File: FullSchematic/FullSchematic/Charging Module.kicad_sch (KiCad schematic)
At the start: 13 parts, among them J1 TP4056

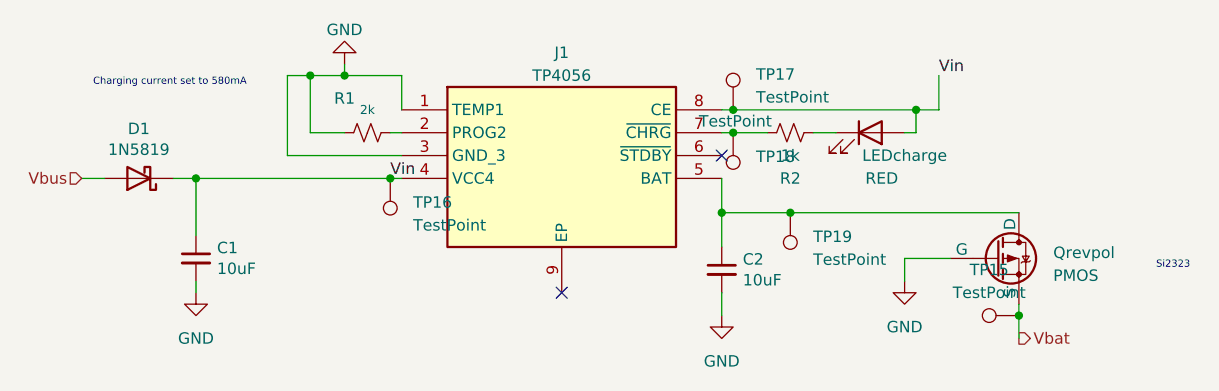
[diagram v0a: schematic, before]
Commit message: completed and generated BOM
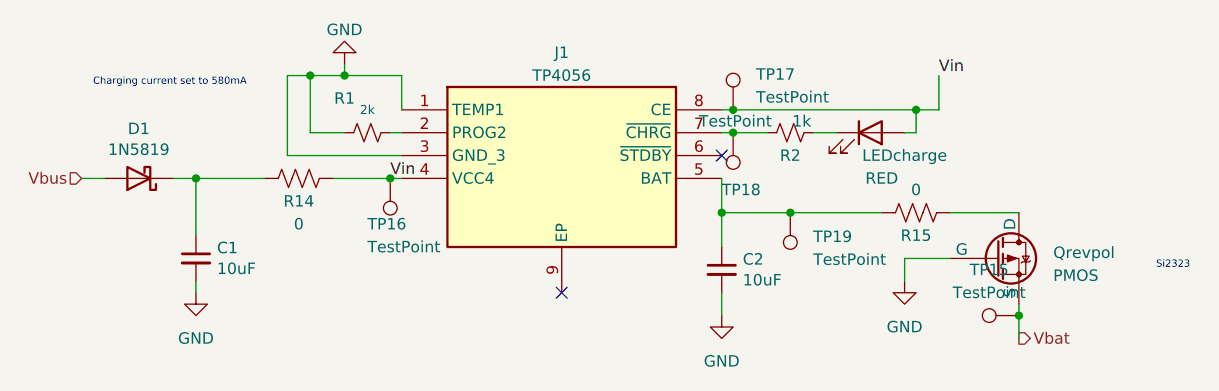
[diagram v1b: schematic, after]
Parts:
- added R14, R15: 0, symbol Device:R_US
- LEDcharge: Price 0.005 -> 0.01; Price ( 1 board) 0.005 -> 0.01; Price (5 boards) 0.025 -> 0.05
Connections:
- net Vin: now also R14.1; no longer C1.1, D1.1 (K)
- net at C2.1, J1.5 (BAT), TP19.1: now also R15.1; no longer Qrevpol.1 (D)
- new net: C1.1, D1.1 (K), R14.2
- new net: Qrevpol.1 (D), R15.2
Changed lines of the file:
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@@
   (junction (at 132.08 67.31) (diameter 0) (color 0 0 0 0)
   )
+  (junction (at 137.16 78.74) (diameter 0) (color 0 0 0 0)
+  )
+  (junction (at 207.01 93.98) (diameter 0) (color 0 0 0 0)
+  )
   (junction (at 181.61 82.55) (diameter 0) (color 0 0 0 0)
   )
-  (junction (at 207.01 93.98) (diameter 0) (color 0 0 0 0)
-  )
-  (junction (at 137.16 78.74) (diameter 0) (color 0 0 0 0)
-  )
   (junction (at 128.27 67.31) (diameter 0) (color 0 0 0 0)
   )
@@
   (junction (at 195.58 71.12) (diameter 0) (color 0 0 0 0)
   )
+  (junction (at 175.26 71.12) (diameter 0) (color 0 0 0 0)
+  )
   (junction (at 115.57 78.74) (diameter 0) (color 0 0 0 0)
-  )
-  (junction (at 175.26 71.12) (diameter 0) (color 0 0 0 0)
   )
   (no_connect (at 173.99 76.2))
@@
     (stroke (width 0) (type default))
   )
+  (wire (pts (xy 137.16 78.74) (xy 138.43 78.74))
+    (stroke (width 0) (type default))
+  )
   (wire (pts (xy 175.26 71.12) (xy 195.58 71.12))
     (stroke (width 0) (type default))
@@
     (stroke (width 0) (type default))
   )
+  (wire (pts (xy 115.57 78.74) (xy 123.19 78.74))
+    (stroke (width 0) (type default))
+  )
   (wire (pts (xy 195.58 73.66) (xy 195.58 71.12))
     (stroke (width 0) (type default))
   )
-  (wire (pts (xy 115.57 78.74) (xy 137.16 78.74))
-    (stroke (width 0) (type default))
-  )
   (wire (pts (xy 138.43 76.2) (xy 125.73 76.2))
     (stroke (width 0) (type default))
@@
     (stroke (width 0) (type default))
   )
+  (wire (pts (xy 199.39 82.55) (xy 207.01 82.55))
+    (stroke (width 0) (type default))
+  )
   (wire (pts (xy 113.03 78.74) (xy 115.57 78.74))
     (stroke (width 0) (type default))
@@
     (stroke (width 0) (type default))
   )
+  (wire (pts (xy 181.61 82.55) (xy 191.77 82.55))
+    (stroke (width 0) (type default))
+  )
   (wire (pts (xy 128.27 73.66) (xy 128.27 67.31))
     (stroke (width 0) (type default))
@@
     (stroke (width 0) (type default))
   )
-  (wire (pts (xy 181.61 82.55) (xy 207.01 82.55))
-    (stroke (width 0) (type default))
-  )
   (wire (pts (xy 194.31 90.17) (xy 194.31 87.63))
     (stroke (width 0) (type default))
@@
     (stroke (width 0) (type default))
   )
-  (wire (pts (xy 137.16 78.74) (xy 138.43 78.74))
+  (wire (pts (xy 130.81 78.74) (xy 137.16 78.74))
     (stroke (width 0) (type default))
   )
@@
     )
   )
+  (symbol (lib_id "Device:R_US") (at 127 78.74 270) (unit 1)
+    (in_bom yes) (on_board yes) (dnp no)
+    (property "Reference" "R14" (at 127 81.28 90)
+      (effects (font (size 1.27 1.27)))
+    )
+    (property "Value" "0" (at 127 83.82 90)
+      (effects (font (size 1.27 1.27)))
+    )
+    (property "Footprint" "" (at 126.746 79.756 90)
+      (effects (font (size 1.27 1.27)) hide)
+    )
+    (property "Datasheet" "~" (at 127 78.74 0)
+      (effects (font (size 1.27 1.27)) hide)
+    )
+    (property "JLCPCB Part #" "C17888" (at 127 78.74 0)
+      (effects (font (size 1.27 1.27)) hide)
+    )
+    (property "Price" "0.003" (at 127 78.74 0)
+      (effects (font (size 1.27 1.27)) hide)
+    )
+    (property "Price ( 1 board)" "0.012" (at 127 78.74 0)
+      (effects (font (size 1.27 1.27)) hide)
+    )
+    (property "Price (5 boards)" "0.06" (at 127 78.74 0)
+      (effects (font (size 1.27 1.27)) hide)
+    )
+    (pin "1")
+    (pin "2")
+    (instances
+      (project "FullSchematic"
+        (path "/5dd86611-a33d-45ee-946c-01c599f30b12/58d1f368-4b84-4dfe-a353-084728cf6b07/00000000-0000-0000-0000-0000640501de"
+          (reference "R14") (unit 1)
+        )
+      )
+    )
+  )
   (symbol (lib_id "Device:LED") (at 190.5 73.66 0) (unit 1)
     (in_bom yes) (on_board yes) (dnp no)
@@
       (effects (font (size 1.27 1.27)) hide)
     )
-    (property "Price ( 1 board)" "0.005" (at 190.5 73.66 0)
-      (effects (font (size 1.27 1.27)) hide)
-    )
-    (property "Price (5 boards)" "0.025" (at 190.5 73.66 0)
+    (property "Price ( 1 board)" "0.01" (at 190.5 73.66 0)
+      (effects (font (size 1.27 1.27)) hide)
+    )
+    (property "Price (5 boards)" "0.05" (at 190.5 73.66 0)
       (effects (font (size 1.27 1.27)) hide)
     )
@@
       (effects (font (size 1.27 1.27)) hide)
     )
-    (property "Price" "0.005" (at 190.5 73.66 0)
+    (property "Price" "0.01" (at 190.5 73.66 0)
       (effects (font (size 1.27 1.27)) hide)
     )
@@
   )
   (symbol (lib_id "Connector:TestPoint") (at 137.16 78.74 180) (unit 1)
-    (in_bom yes) (on_board yes) (dnp no) (fields_autoplaced)
-    (property "Reference" "TP16" (at 139.7 81.407 0)
+    (in_bom yes) (on_board yes) (dnp no)
+    (property "Reference" "TP16" (at 134.62 83.82 0)
       (effects (font (size 1.27 1.27)) (justify right))
     )
-    (property "Value" "TestPoint" (at 139.7 83.947 0)
+    (property "Value" "TestPoint" (at 134.62 86.36 0)
       (effects (font (size 1.27 1.27)) (justify right))
     )
@@
     )
   )
+  (symbol (lib_id "Device:R_US") (at 195.58 82.55 90) (unit 1)
+    (in_bom yes) (on_board yes) (dnp no)
+    (property "Reference" "R15" (at 195.58 85.09 90)
+      (effects (font (size 1.27 1.27)))
+    )
+    (property "Value" "0" (at 195.58 80.01 90)
+      (effects (font (size 1.27 1.27)))
+    )
+    (property "Footprint" "" (at 195.834 81.534 90)
+      (effects (font (size 1.27 1.27)) hide)
+    )
+    (property "Datasheet" "~" (at 195.58 82.55 0)
+      (effects (font (size 1.27 1.27)) hide)
+    )
+    (property "JLCPCB Part #" "C17888" (at 195.58 82.55 0)
+      (effects (font (size 1.27 1.27)) hide)
+    )
+    (property "Price" "0.003" (at 195.58 82.55 0)
+      (effects (font (size 1.27 1.27)) hide)
+    )
+    (property "Price ( 1 board)" "0.012" (at 195.58 82.55 0)
+      (effects (font (size 1.27 1.27)) hide)
+    )
+    (property "Price (5 boards)" "0.06" (at 195.58 82.55 0)
+      (effects (font (size 1.27 1.27)) hide)
+    )
+    (pin "1")
+    (pin "2")
+    (instances
+      (project "FullSchematic"
+        (path "/5dd86611-a33d-45ee-946c-01c599f30b12/58d1f368-4b84-4dfe-a353-084728cf6b07/00000000-0000-0000-0000-0000640501de"
+          (reference "R15") (unit 1)
+        )
+      )
+    )
+  )
   (symbol (lib_id "power:GND") (at 115.57 91.44 0) (unit 1)
     (in_bom yes) (on_board yes) (dnp no) (fields_autoplaced)
@@
   (symbol (lib_id "Device:R_Small_US") (at 181.61 73.66 90) (unit 1)
     (in_bom yes) (on_board yes) (dnp no)
-    (property "Reference" "R2" (at 181.61 78.74 90)
-      (effects (font (size 1.27 1.27)))
-    )
-    (property "Value" "1k" (at 181.61 76.2 90)
+    (property "Reference" "R2" (at 181.61 76.2 90)
+      (effects (font (size 1.27 1.27)))
+    )
+    (property "Value" "1k" (at 182.88 72.39 90)
       (effects (font (size 1.27 1.27)))
     )
@@
   (symbol (lib_id "Connector:TestPoint") (at 175.26 73.66 180) (unit 1)
     (in_bom yes) (on_board yes) (dnp no)
-    (property "Reference" "TP18" (at 177.8 76.327 0)
+    (property "Reference" "TP18" (at 173.99 80.01 0)
       (effects (font (size 1.27 1.27)) (justify right))
     )

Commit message: added more footprints
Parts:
- R14, R15: footprint (none) -> SpecificFootprints:RESC2013X65N
- TP15, TP16, TP17, TP18, TP19: footprint (none) -> TestPoint:TestPoint_Pad_D2.0mm
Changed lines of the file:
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@@
       (effects (font (size 1.27 1.27)))
     )
-    (property "Footprint" "" (at 126.746 79.756 90)
+    (property "Footprint" "SpecificFootprints:RESC2013X65N" (at 126.746 79.756 90)
       (effects (font (size 1.27 1.27)) hide)
     )
@@
       (effects (font (size 1.27 1.27)) (justify left))
     )
-    (property "Footprint" "" (at 180.34 71.12 0)
+    (property "Footprint" "TestPoint:TestPoint_Pad_D2.0mm" (at 180.34 71.12 0)
       (effects (font (size 1.27 1.27)) hide)
     )
@@
       (effects (font (size 1.27 1.27)) (justify right))
     )
-    (property "Footprint" "" (at 132.08 78.74 0)
+    (property "Footprint" "TestPoint:TestPoint_Pad_D2.0mm" (at 132.08 78.74 0)
       (effects (font (size 1.27 1.27)) hide)
     )
@@
       (effects (font (size 1.27 1.27)))
     )
-    (property "Footprint" "" (at 207.01 88.9 0)
+    (property "Footprint" "TestPoint:TestPoint_Pad_D2.0mm" (at 207.01 88.9 0)
       (effects (font (size 1.27 1.27)) hide)
     )
@@
       (effects (font (size 1.27 1.27)))
     )
-    (property "Footprint" "" (at 195.834 81.534 90)
+    (property "Footprint" "SpecificFootprints:RESC2013X65N" (at 195.834 81.534 90)
       (effects (font (size 1.27 1.27)) hide)
     )
@@
       (effects (font (size 1.27 1.27)) (justify right))
     )
-    (property "Footprint" "" (at 176.53 82.55 0)
+    (property "Footprint" "TestPoint:TestPoint_Pad_D2.0mm" (at 176.53 82.55 0)
       (effects (font (size 1.27 1.27)) hide)
     )
@@
       (effects (font (size 1.27 1.27)) (justify right))
     )
-    (property "Footprint" "" (at 170.18 73.66 0)
-      (effects (font (size 1.27 1.27)) hide)
-    )
+    (property "Footprint" "TestPoint:TestPoint_Pad_D2.0mm" (at 170.18 73.66 0)
+      (effects (font (size 1.27 1.27)) hide)
+    )

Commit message: tried to go to previous version
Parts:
- C1, C2: footprint CL10A475KO8NNNC -> SpecificFootprints:CAPC1608X90N
- D1: footprint Diode_THT:D_DO-41_SOD81_P10.16mm_Horizontal -> SpecificFootprints:DIOAD1405W86L465D235
- LEDcharge: footprint (none) -> LED_THT:LED_D5.0mm_IRBlack
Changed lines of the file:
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@@
       (effects (font (size 1.27 1.27)) (justify left))
     )
-    (property "Footprint" "CL10A475KO8NNNC" (at 115.57 87.63 0)
+    (property "Footprint" "SpecificFootprints:CAPC1608X90N" (at 115.57 87.63 0)
       (effects (font (size 1.27 1.27)) hide)
     )
@@
       (effects (font (size 1.27 1.27)) (justify left))
     )
-    (property "Footprint" "CL10A475KO8NNNC" (at 173.99 88.9 0)
+    (property "Footprint" "SpecificFootprints:CAPC1608X90N" (at 173.99 88.9 0)
       (effects (font (size 1.27 1.27)) hide)
     )
@@
       (effects (font (size 1.27 1.27)))
     )
-    (property "Footprint" "Diode_THT:D_DO-41_SOD81_P10.16mm_Horizontal" (at 109.22 74.295 0)
+    (property "Footprint" "SpecificFootprints:DIOAD1405W86L465D235" (at 109.22 74.295 0)
       (effects (font (size 1.27 1.27)) hide)
     )
@@
       (effects (font (size 1.27 1.27)))
     )
-    (property "Footprint" "" (at 190.5 73.66 0)
-      (effects (font (size 1.27 1.27)) hide)
-    )
+    (property "Footprint" "LED_THT:LED_D5.0mm_IRBlack" (at 190.5 73.66 0)
+      (effects (font (size 1.27 1.27)) hide)
+    )

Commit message: Aimee
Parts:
- R14, R15: footprint SpecificFootprints:RESC2013X65N -> (none)
- TP15, TP16, TP17, TP18, TP19: footprint TestPoint:TestPoint_Pad_D2.0mm -> (none)
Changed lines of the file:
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@@
       (effects (font (size 1.27 1.27)))
     )
-    (property "Footprint" "SpecificFootprints:RESC2013X65N" (at 126.746 79.756 90)
+    (property "Footprint" "" (at 126.746 79.756 90)
       (effects (font (size 1.27 1.27)) hide)
     )
@@
       (effects (font (size 1.27 1.27)) (justify left))
     )
-    (property "Footprint" "TestPoint:TestPoint_Pad_D2.0mm" (at 180.34 71.12 0)
+    (property "Footprint" "" (at 180.34 71.12 0)
       (effects (font (size 1.27 1.27)) hide)
     )
@@
       (effects (font (size 1.27 1.27)) (justify right))
     )
-    (property "Footprint" "TestPoint:TestPoint_Pad_D2.0mm" (at 132.08 78.74 0)
+    (property "Footprint" "" (at 132.08 78.74 0)
       (effects (font (size 1.27 1.27)) hide)
     )
@@
       (effects (font (size 1.27 1.27)))
     )
-    (property "Footprint" "TestPoint:TestPoint_Pad_D2.0mm" (at 207.01 88.9 0)
+    (property "Footprint" "" (at 207.01 88.9 0)
       (effects (font (size 1.27 1.27)) hide)
     )
@@
       (effects (font (size 1.27 1.27)))
     )
-    (property "Footprint" "SpecificFootprints:RESC2013X65N" (at 195.834 81.534 90)
+    (property "Footprint" "" (at 195.834 81.534 90)
       (effects (font (size 1.27 1.27)) hide)
     )
@@
       (effects (font (size 1.27 1.27)) (justify right))
     )
-    (property "Footprint" "TestPoint:TestPoint_Pad_D2.0mm" (at 176.53 82.55 0)
+    (property "Footprint" "" (at 176.53 82.55 0)
       (effects (font (size 1.27 1.27)) hide)
     )
@@
       (effects (font (size 1.27 1.27)) (justify right))
     )
-    (property "Footprint" "TestPoint:TestPoint_Pad_D2.0mm" (at 170.18 73.66 0)
-      (effects (font (size 1.27 1.27)) hide)
-    )
+    (property "Footprint" "" (at 170.18 73.66 0)
+      (effects (font (size 1.27 1.27)) hide)
+    )

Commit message: Opening MicroController
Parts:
- C1, C2: footprint SpecificFootprints:CAPC1608X90N -> CL10A475KO8NNNC
- D1: footprint SpecificFootprints:DIOAD1405W86L465D235 -> Diode_THT:D_DO-41_SOD81_P10.16mm_Horizontal
- LEDcharge: footprint LED_THT:LED_D5.0mm_IRBlack -> (none)
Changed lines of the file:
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@@
       (effects (font (size 1.27 1.27)) (justify left))
     )
-    (property "Footprint" "SpecificFootprints:CAPC1608X90N" (at 115.57 87.63 0)
+    (property "Footprint" "CL10A475KO8NNNC" (at 115.57 87.63 0)
       (effects (font (size 1.27 1.27)) hide)
     )
@@
       (effects (font (size 1.27 1.27)) (justify left))
     )
-    (property "Footprint" "SpecificFootprints:CAPC1608X90N" (at 173.99 88.9 0)
+    (property "Footprint" "CL10A475KO8NNNC" (at 173.99 88.9 0)
       (effects (font (size 1.27 1.27)) hide)
     )
@@
       (effects (font (size 1.27 1.27)))
     )
-    (property "Footprint" "SpecificFootprints:DIOAD1405W86L465D235" (at 109.22 74.295 0)
+    (property "Footprint" "Diode_THT:D_DO-41_SOD81_P10.16mm_Horizontal" (at 109.22 74.295 0)
       (effects (font (size 1.27 1.27)) hide)
     )
@@
       (effects (font (size 1.27 1.27)))
     )
-    (property "Footprint" "LED_THT:LED_D5.0mm_IRBlack" (at 190.5 73.66 0)
-      (effects (font (size 1.27 1.27)) hide)
-    )
+    (property "Footprint" "" (at 190.5 73.66 0)
+      (effects (font (size 1.27 1.27)) hide)
+    )

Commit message: resetting
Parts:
- C1, C2: footprint CL10A475KO8NNNC -> SpecificFootprints:CAPC1608X90N
- D1: footprint Diode_THT:D_DO-41_SOD81_P10.16mm_Horizontal -> SpecificFootprints:DIOAD1405W86L465D235
- LEDcharge: footprint (none) -> LED_THT:LED_D5.0mm_IRBlack
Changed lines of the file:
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@@
       (effects (font (size 1.27 1.27)) (justify left))
     )
-    (property "Footprint" "CL10A475KO8NNNC" (at 115.57 87.63 0)
+    (property "Footprint" "SpecificFootprints:CAPC1608X90N" (at 115.57 87.63 0)
       (effects (font (size 1.27 1.27)) hide)
     )
@@
       (effects (font (size 1.27 1.27)) (justify left))
     )
-    (property "Footprint" "CL10A475KO8NNNC" (at 173.99 88.9 0)
+    (property "Footprint" "SpecificFootprints:CAPC1608X90N" (at 173.99 88.9 0)
       (effects (font (size 1.27 1.27)) hide)
     )
@@
       (effects (font (size 1.27 1.27)))
     )
-    (property "Footprint" "Diode_THT:D_DO-41_SOD81_P10.16mm_Horizontal" (at 109.22 74.295 0)
+    (property "Footprint" "SpecificFootprints:DIOAD1405W86L465D235" (at 109.22 74.295 0)
       (effects (font (size 1.27 1.27)) hide)
     )
@@
       (effects (font (size 1.27 1.27)))
     )
-    (property "Footprint" "" (at 190.5 73.66 0)
-      (effects (font (size 1.27 1.27)) hide)
-    )
+    (property "Footprint" "LED_THT:LED_D5.0mm_IRBlack" (at 190.5 73.66 0)
+      (effects (font (size 1.27 1.27)) hide)
+    )

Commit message: adding of all footprints
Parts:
- C1, C2: footprint SpecificFootprints:CAPC1608X90N -> Library:CAPC1608X90N
- D1: footprint SpecificFootprints:DIOAD1405W86L465D235 -> Library:DIOAD1405W86L465D235
- J1: footprint SOIC127P600X175-9N -> Library:SOIC127P600X175-9N
- LEDcharge: footprint LED_THT:LED_D5.0mm_IRBlack -> LED_THT:LED_D3.0mm_IRBlack
- Qrevpol: footprint (none) -> Library:SOT95P237X112-3N
- R1, R14, R15, R2: footprint (none) -> Library:RESC2013X65N
- TP15, TP16, TP17, TP18, TP19: footprint (none) -> TestPoint:TestPoint_Pad_D2.0mm
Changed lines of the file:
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@@
       (effects (font (size 1.27 1.27)) (justify left))
     )
-    (property "Footprint" "SpecificFootprints:CAPC1608X90N" (at 115.57 87.63 0)
+    (property "Footprint" "Library:CAPC1608X90N" (at 115.57 87.63 0)
       (effects (font (size 1.27 1.27)) hide)
     )
@@
       (effects (font (size 1.27 1.27)) (justify left))
     )
-    (property "Footprint" "SpecificFootprints:CAPC1608X90N" (at 173.99 88.9 0)
+    (property "Footprint" "Library:CAPC1608X90N" (at 173.99 88.9 0)
       (effects (font (size 1.27 1.27)) hide)
     )
@@
       (effects (font (size 1.27 1.27)))
     )
-    (property "Footprint" "SpecificFootprints:DIOAD1405W86L465D235" (at 109.22 74.295 0)
+    (property "Footprint" "Library:DIOAD1405W86L465D235" (at 109.22 74.295 0)
       (effects (font (size 1.27 1.27)) hide)
     )
@@
       (effects (font (size 1 1)))
     )
-    (property "Footprint" "" (at 134.62 73.66 0)
+    (property "Footprint" "Library:RESC2013X65N" (at 134.62 73.66 0)
       (effects (font (size 1.27 1.27)) hide)
     )
@@
       (effects (font (size 1.27 1.27)))
     )
-    (property "Footprint" "" (at 126.746 79.756 90)
+    (property "Footprint" "Library:RESC2013X65N" (at 126.746 79.756 90)
       (effects (font (size 1.27 1.27)) hide)
     )
@@
       (effects (font (size 1.27 1.27)))
     )
-    (property "Footprint" "LED_THT:LED_D5.0mm_IRBlack" (at 190.5 73.66 0)
+    (property "Footprint" "LED_THT:LED_D3.0mm_IRBlack" (at 190.5 73.66 0)
       (effects (font (size 1.27 1.27)) hide)
     )
@@
       (effects (font (size 1.27 1.27)) (justify left))
     )
-    (property "Footprint" "" (at 180.34 71.12 0)
+    (property "Footprint" "TestPoint:TestPoint_Pad_D2.0mm" (at 180.34 71.12 0)
       (effects (font (size 1.27 1.27)) hide)
     )
@@
       (effects (font (size 1.27 1.27)) (justify right))
     )
-    (property "Footprint" "" (at 132.08 78.74 0)
+    (property "Footprint" "TestPoint:TestPoint_Pad_D2.0mm" (at 132.08 78.74 0)
       (effects (font (size 1.27 1.27)) hide)
     )
@@
       (effects (font (size 1.27 1.27)))
     )
-    (property "Footprint" "SOIC127P600X175-9N" (at 170.18 166.04 0)
+    (property "Footprint" "Library:SOIC127P600X175-9N" (at 170.18 166.04 0)
       (effects (font (size 1.27 1.27)) (justify left top) hide)
     )
@@
       (effects (font (size 1.27 1.27)))
     )
-    (property "Footprint" "" (at 207.01 88.9 0)
+    (property "Footprint" "TestPoint:TestPoint_Pad_D2.0mm" (at 207.01 88.9 0)
       (effects (font (size 1.27 1.27)) hide)
     )
@@
       (effects (font (size 1.27 1.27)))
     )
-    (property "Footprint" "" (at 195.834 81.534 90)
+    (property "Footprint" "Library:RESC2013X65N" (at 195.834 81.534 90)
       (effects (font (size 1.27 1.27)) hide)
     )
@@
       (effects (font (size 1.27 1.27)))
     )
-    (property "Footprint" "" (at 181.61 73.66 0)
+    (property "Footprint" "Library:RESC2013X65N" (at 181.61 73.66 0)
       (effects (font (size 1.27 1.27)) hide)
     )
@@
       (effects (font (size 1.27 1.27)) (justify right))
     )
-    (property "Footprint" "" (at 176.53 82.55 0)
+    (property "Footprint" "TestPoint:TestPoint_Pad_D2.0mm" (at 176.53 82.55 0)
       (effects (font (size 1.27 1.27)) hide)
     )
@@
       (effects (font (size 1.27 1.27)) (justify left))
     )
-    (property "Footprint" "" (at 209.55 85.09 0)
+    (property "Footprint" "Library:SOT95P237X112-3N" (at 209.55 85.09 0)
       (effects (font (size 1.27 1.27)) hide)
     )
@@
       (effects (font (size 1.27 1.27)) (justify right))
     )
-    (property "Footprint" "" (at 170.18 73.66 0)
-      (effects (font (size 1.27 1.27)) hide)
-    )
+    (property "Footprint" "TestPoint:TestPoint_Pad_D2.0mm" (at 170.18 73.66 0)
+      (effects (font (size 1.27 1.27)) hide)
+    )
